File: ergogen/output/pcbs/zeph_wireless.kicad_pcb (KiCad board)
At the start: 2 copper layers, 130.3 x 107.9 mm, 120 parts

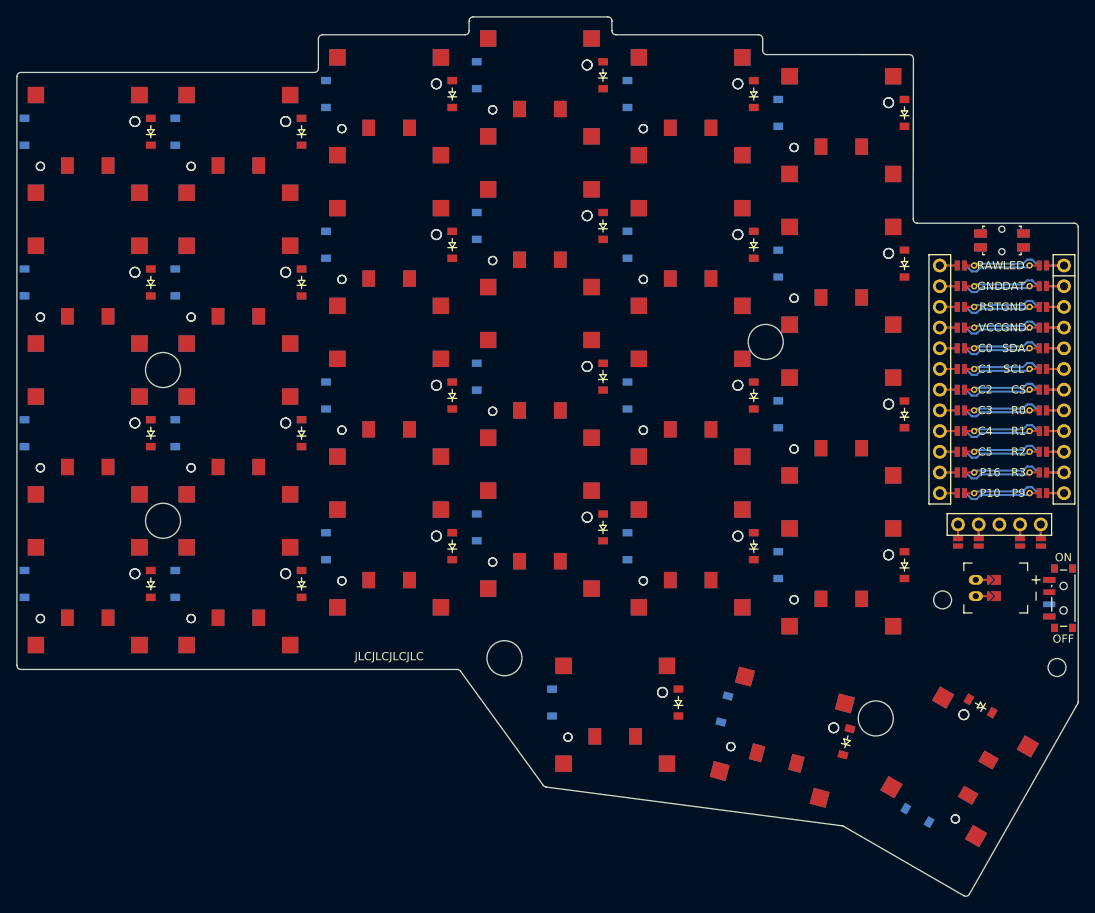
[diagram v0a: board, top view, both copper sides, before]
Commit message: feat: reversible pg1316s switch footprint
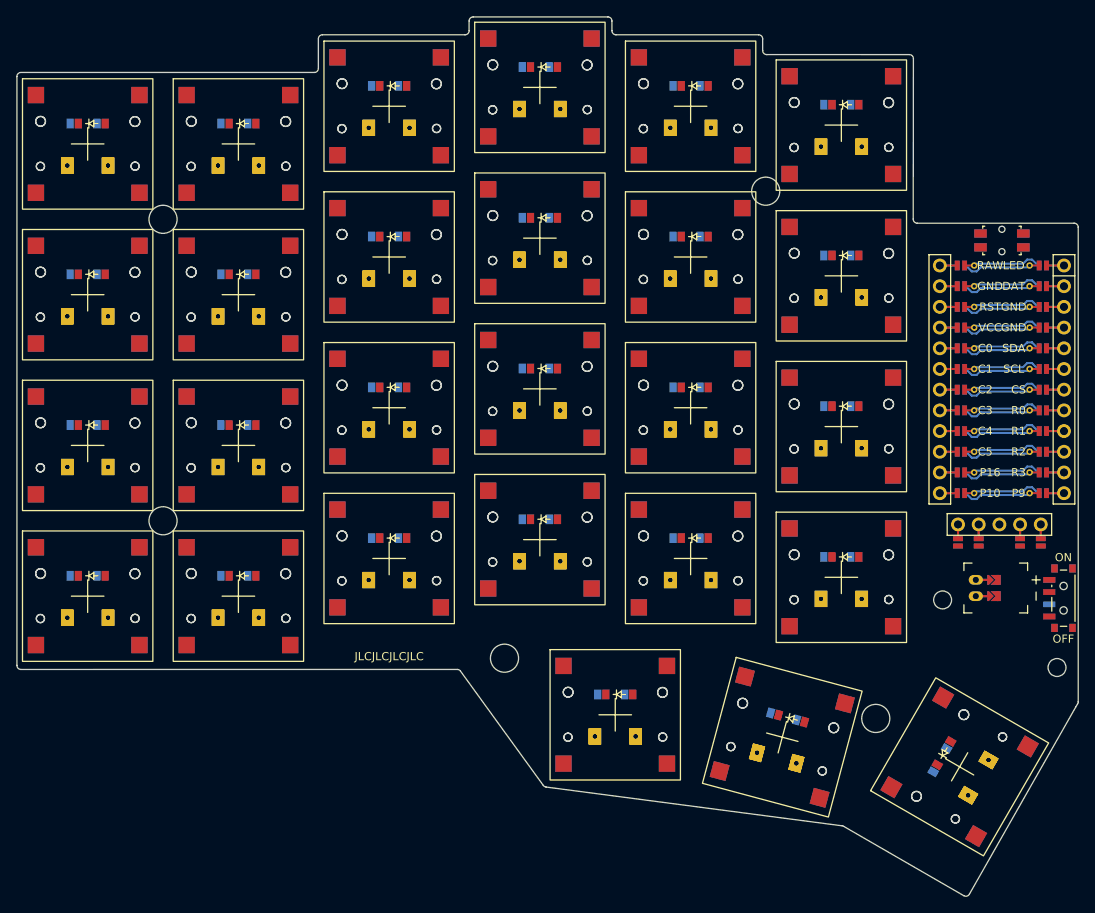
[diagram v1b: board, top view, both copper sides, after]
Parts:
- S1, S10, S11, S12, S13, S14, S15, S16, S17, S18, S19, S2, S20, S21, S22, S23, S24, S25, S26, S27, S28, S29, S3, S30, S31, S32, S33, S34, S35, S36, S37, S38, S39, S4, S40, S41, S42, S43, S44, S45, S46, S47, S48, S49, S5, S50, S51, S52, S53, S54, S6, S7, S8, S9: footprint CPG1316S01D02_mikeholscher -> CPG1316S01D02
- moved MH3 18.5 mm to (109.2, 53.8)
- moved MH5 18.5 mm to (183.2, 50.3)
- moved D27 7.32 mm to (204.6, 120.1), turned to 60 degrees
- moved D54 7.32 mm to (205.1, 119.3), turned to 60 degrees
- moved D26 7.32 mm to (185.4, 114.8), turned to -15 degrees
- moved D53 7.32 mm to (186.4, 115.0), turned to -15 degrees
- moved D1 7.32 mm to (99.5, 97.5), turned to 0 degrees
- moved D10 7.32 mm to (136.5, 74.4), turned to 0 degrees
- moved D11 7.32 mm to (136.5, 55.9), turned to 0 degrees
- moved D12 7.32 mm to (136.5, 37.4), turned to 0 degrees
- moved D13 7.32 mm to (155.0, 90.6), turned to 0 degrees
- moved D14 7.32 mm to (155.0, 72.1), turned to 0 degrees
- moved D15 7.32 mm to (155.0, 53.6), turned to 0 degrees
- moved D16 7.32 mm to (155.0, 35.1), turned to 0 degrees
- moved D17 7.32 mm to (173.5, 92.9), turned to 0 degrees
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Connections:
- S1 pad 1: outer_bottom_B -> C0
- S1 pad 2: C0 -> outer_bottom_B
- S10 pad 1: ring_home_B -> C2
- S10 pad 2: C2 -> ring_home_B
- S11 pad 1: ring_top_B -> C2
- S11 pad 2: C2 -> ring_top_B
- S12 pad 1: ring_numbers_B -> C2
- S12 pad 2: C2 -> ring_numbers_B
- S13 pad 1: middle_bottom_B -> C3
- S13 pad 2: C3 -> middle_bottom_B
- S14 pad 1: middle_home_B -> C3
- S14 pad 2: C3 -> middle_home_B
- S15 pad 1: middle_top_B -> C3
- S15 pad 2: C3 -> middle_top_B
- S16 pad 1: middle_numbers_B -> C3
- S16 pad 2: C3 -> middle_numbers_B
- S17 pad 1: index_bottom_B -> C4
- S17 pad 2: C4 -> index_bottom_B
- S18 pad 1: index_home_B -> C4
- S18 pad 2: C4 -> index_home_B
- S19 pad 1: index_top_B -> C4
- S19 pad 2: C4 -> index_top_B
- S2 pad 1: outer_home_B -> C0
- S2 pad 2: C0 -> outer_home_B
- S20 pad 1: index_numbers_B -> C4
- S20 pad 2: C4 -> index_numbers_B
- S21 pad 1: inner_bottom_B -> C5
- S21 pad 2: C5 -> inner_bottom_B
- S22 pad 1: inner_home_B -> C5
- S22 pad 2: C5 -> inner_home_B
- S23 pad 1: inner_top_B -> C5
- S23 pad 2: C5 -> inner_top_B
- S24 pad 1: inner_numbers_B -> C5
- S24 pad 2: C5 -> inner_numbers_B
- S25 pad 1: near_home_B -> C3
- S25 pad 2: C3 -> near_home_B
- S26 pad 1: mid_home_B -> C4
- S26 pad 2: C4 -> mid_home_B
- S27 pad 1: far_home_B -> C5
- S27 pad 2: C5 -> far_home_B
- S28 pad 1: outer_bottom_F -> C0
- S28 pad 2: C0 -> outer_bottom_F
- S29 pad 1: outer_home_F -> C0
- S29 pad 2: C0 -> outer_home_F
- S3 pad 1: outer_top_B -> C0
- S3 pad 2: C0 -> outer_top_B
- S30 pad 1: outer_top_F -> C0
- S30 pad 2: C0 -> outer_top_F
- S31 pad 1: outer_numbers_F -> C0
- S31 pad 2: C0 -> outer_numbers_F
- S32 pad 1: pinky_bottom_F -> C1
- S32 pad 2: C1 -> pinky_bottom_F
- S33 pad 1: pinky_home_F -> C1
- S33 pad 2: C1 -> pinky_home_F
- S34 pad 1: pinky_top_F -> C1
- S34 pad 2: C1 -> pinky_top_F
- S35 pad 1: pinky_numbers_F -> C1
- S35 pad 2: C1 -> pinky_numbers_F
- S36 pad 1: ring_bottom_F -> C2
- S36 pad 2: C2 -> ring_bottom_F
- S37 pad 1: ring_home_F -> C2
- S37 pad 2: C2 -> ring_home_F
- S38 pad 1: ring_top_F -> C2
- S38 pad 2: C2 -> ring_top_F
- S39 pad 1: ring_numbers_F -> C2
- S39 pad 2: C2 -> ring_numbers_F
- S4 pad 1: outer_numbers_B -> C0
- S4 pad 2: C0 -> outer_numbers_B
- S40 pad 1: middle_bottom_F -> C3
- S40 pad 2: C3 -> middle_bottom_F
- S41 pad 1: middle_home_F -> C3
- S41 pad 2: C3 -> middle_home_F
- S42 pad 1: middle_top_F -> C3
- S42 pad 2: C3 -> middle_top_F
- S43 pad 1: middle_numbers_F -> C3
- S43 pad 2: C3 -> middle_numbers_F
- S44 pad 1: index_bottom_F -> C4
- S44 pad 2: C4 -> index_bottom_F
- S45 pad 1: index_home_F -> C4
- S45 pad 2: C4 -> index_home_F
- S46 pad 1: index_top_F -> C4
- S46 pad 2: C4 -> index_top_F
- S47 pad 1: index_numbers_F -> C4
- S47 pad 2: C4 -> index_numbers_F
- S48 pad 1: inner_bottom_F -> C5
- S48 pad 2: C5 -> inner_bottom_F
- S49 pad 1: inner_home_F -> C5
- S49 pad 2: C5 -> inner_home_F
- S5 pad 1: pinky_bottom_B -> C1
- S5 pad 2: C1 -> pinky_bottom_B
- S50 pad 1: inner_top_F -> C5
- S50 pad 2: C5 -> inner_top_F
- S51 pad 1: inner_numbers_F -> C5
- S51 pad 2: C5 -> inner_numbers_F
- S52 pad 1: near_home_F -> C3
- S52 pad 2: C3 -> near_home_F
- S53 pad 1: mid_home_F -> C4
- S53 pad 2: C4 -> mid_home_F
- S54 pad 1: far_home_F -> C5
- S54 pad 2: C5 -> far_home_F
- S6 pad 1: pinky_home_B -> C1
- S6 pad 2: C1 -> pinky_home_B
- S7 pad 1: pinky_top_B -> C1
- S7 pad 2: C1 -> pinky_top_B
- S8 pad 1: pinky_numbers_B -> C1
- S8 pad 2: C1 -> pinky_numbers_B
- S9 pad 1: ring_bottom_B -> C2
- S9 pad 2: C2 -> ring_bottom_B

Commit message: fix: pg1316s pads cannot be tht on reversible pcb
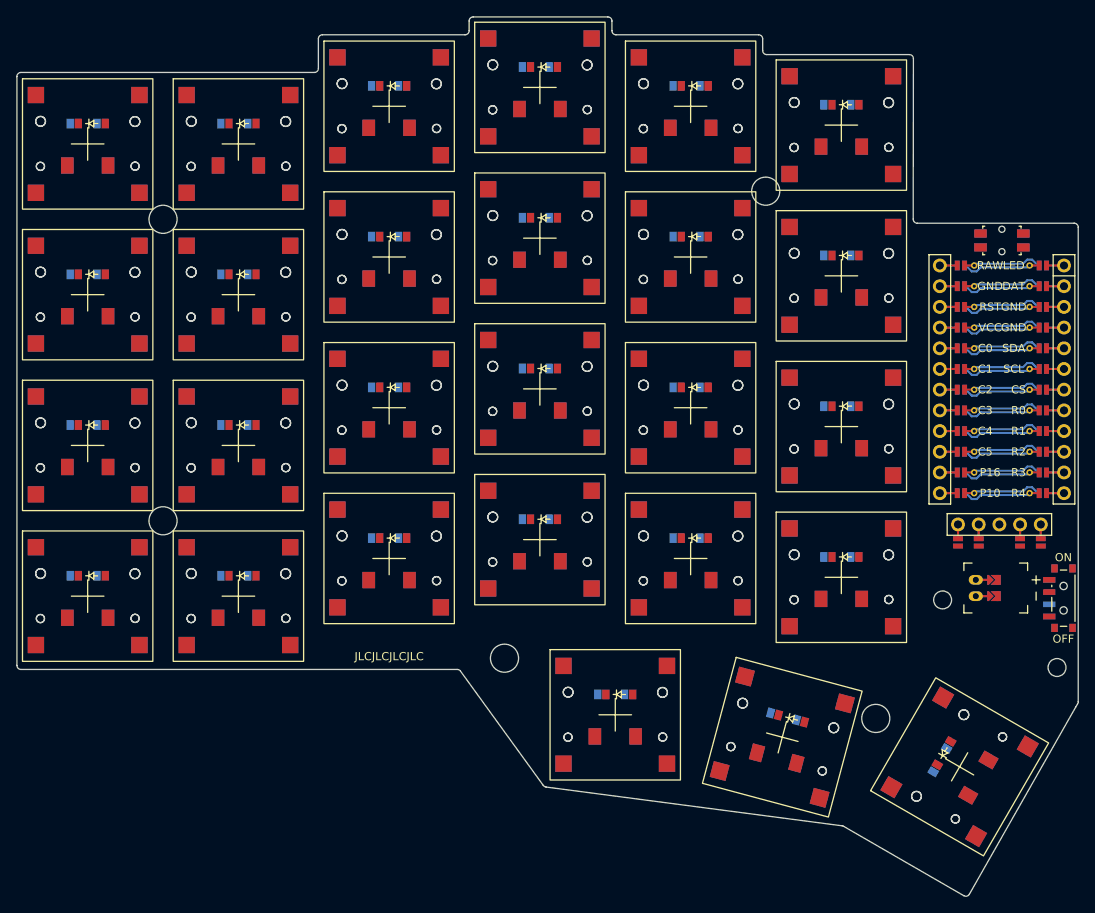
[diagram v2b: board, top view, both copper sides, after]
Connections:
- D25 pad 1: R3 -> R4
- D26 pad 1: R3 -> R4
- D27 pad 1: R3 -> R4
- D52 pad 1: R3 -> R4
- D53 pad 1: R3 -> R4
- D54 pad 1: R3 -> R4
- MCU1 pad 112: P9 -> R4

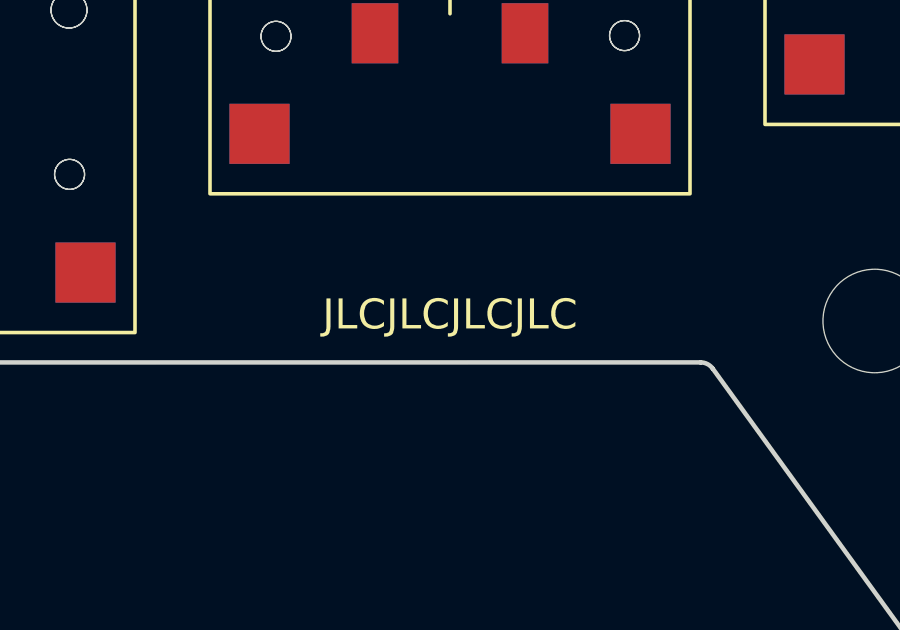
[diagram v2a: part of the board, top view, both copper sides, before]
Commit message: feat: board text
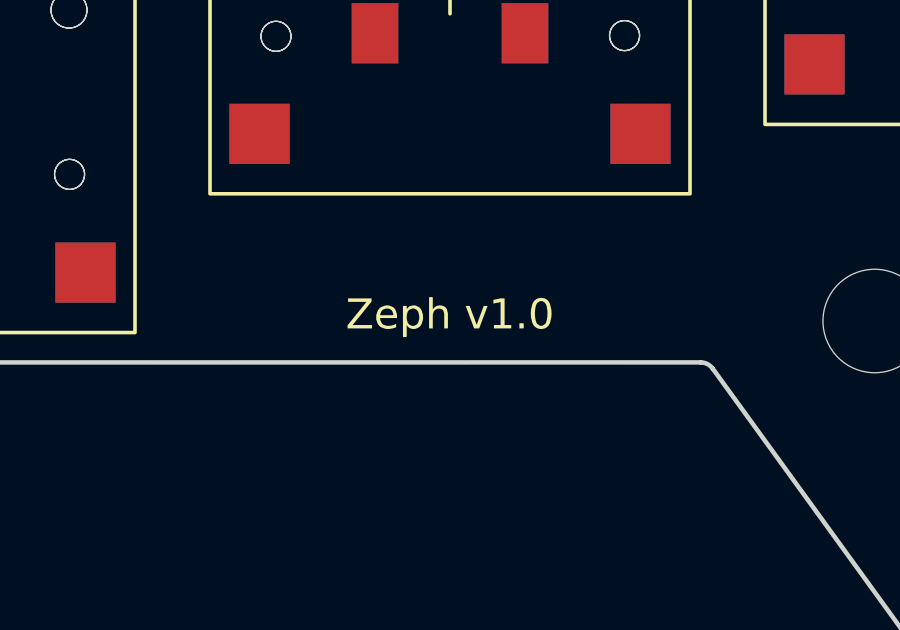
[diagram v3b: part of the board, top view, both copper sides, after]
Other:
- board text added: "Zeph v1.0"
- board text removed: "JLCJLCJLCJLC"
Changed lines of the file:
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@@
   (segment (start 215.90430500000002 86.635) (end 215.303695 86.635) (width 0.25) (layer "B.Cu"))
   (segment (start 215.303695 86.635) (end 214.798695 87.14) (width 0.25) (layer "B.Cu"))
-  (gr_text "JLCJLCJLCJLC"
+  (gr_text "Zeph v1.0"
     (at 137 107.4 0)
     (layer "F.SilkS" )
@@
     )
   )
-  (gr_text "JLCJLCJLCJLC"
+  (gr_text "Zeph v1.0"
     (at 137 107.4 0)
     (layer "B.SilkS" )
